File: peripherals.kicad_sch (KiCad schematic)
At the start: 10 parts, among them J10 perslot3ad, J11 perslot4ad, J12 perslot3c, J13 perslot4c, J14 peridcad, J15 peridcc, J6 perslot1ad, J7 perslot1c, J8 perslot2ad, J9 perslot2c

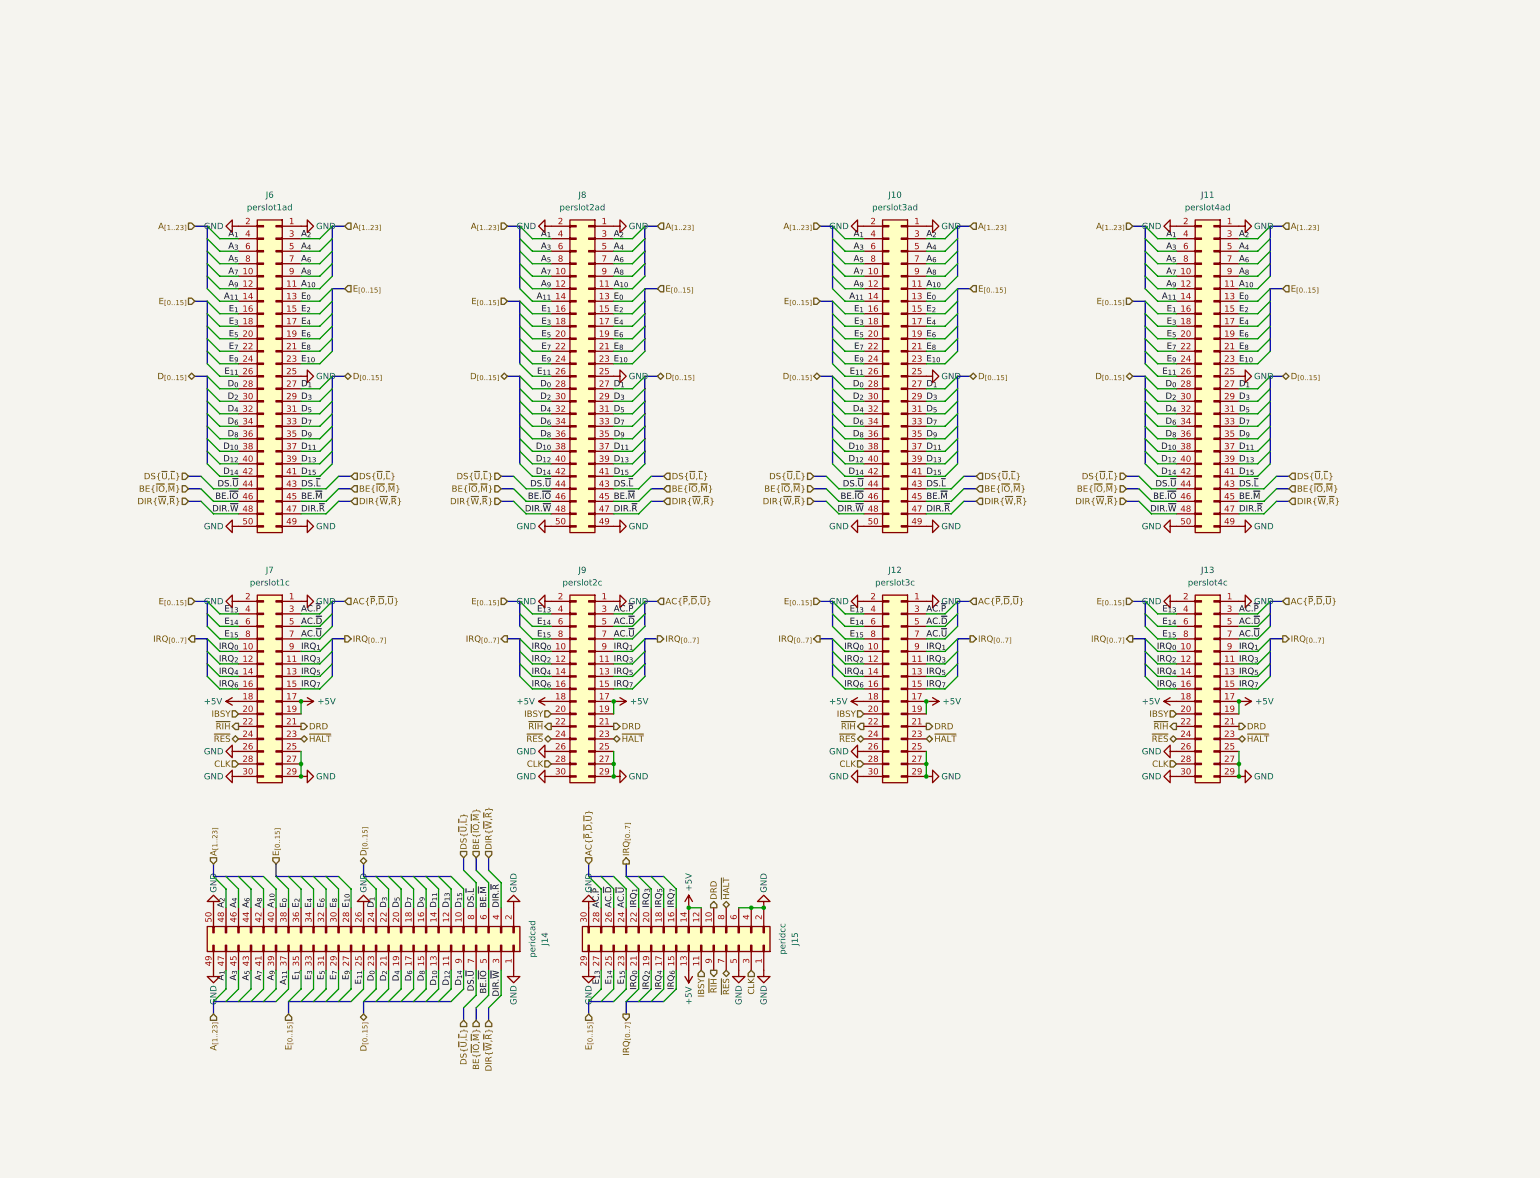
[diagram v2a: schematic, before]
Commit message: first commit: scheme ok [decoder]: 	- new spv. address space [mmu]: 	- removed pidreg 	- switched back to 8Kb mmu rams [ram/peripherals]: 	- added ground pins to connectors [misc]: 	- added DMA support 	- added clock halfer
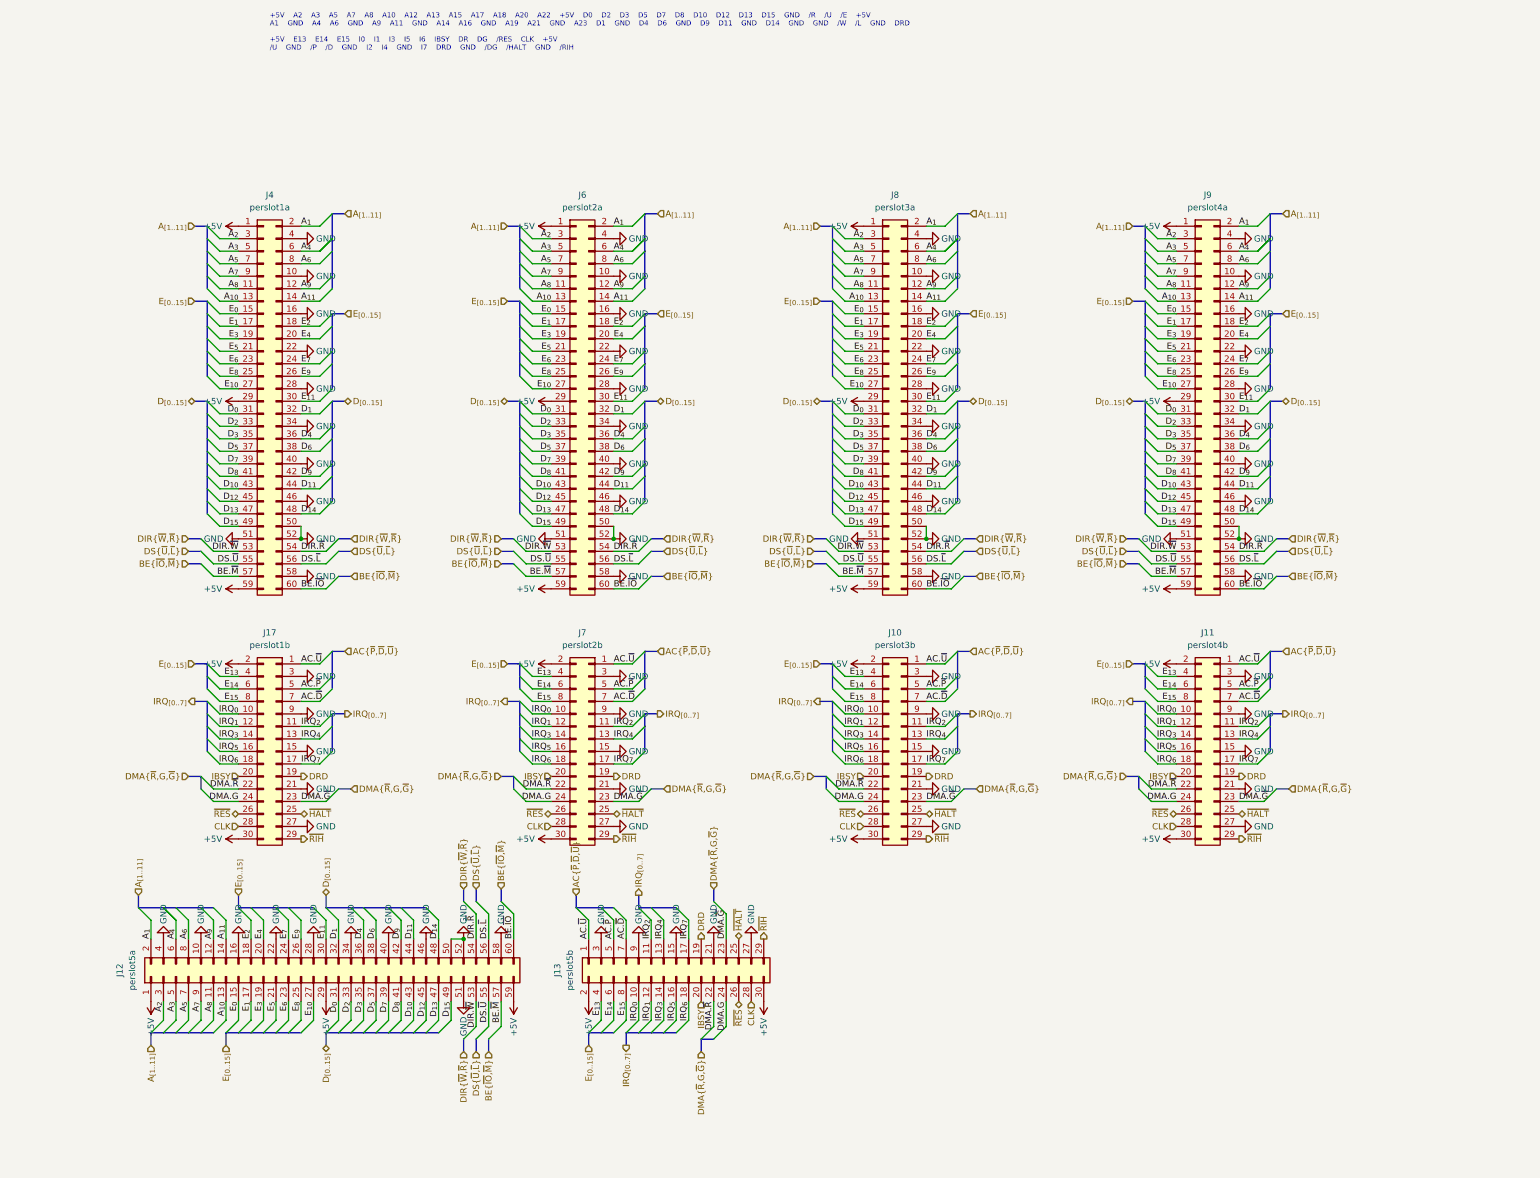
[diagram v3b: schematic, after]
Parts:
- removed J10: perslot3ad, Connector_PCBEdge:TE_1-5530843-6, symbol Connector_Generic:Conn_02x25_Odd_Even
- removed J11: perslot4ad, Connector_PCBEdge:TE_1-5530843-6, symbol Connector_Generic:Conn_02x25_Odd_Even
- removed J12: perslot3c, Connector_PCBEdge:55308432, symbol Connector_Generic:Conn_02x15_Odd_Even
- removed J14: peridcad, Connector_IDC:IDC-Header_2x25_P2.54mm_Horizontal, symbol Connector_Generic:Conn_02x25_Odd_Even
- removed J15: peridcc, Connector_IDC:IDC-Header_2x15_P2.54mm_Horizontal, symbol Connector_Generic:Conn_02x15_Odd_Even
- removed J6: perslot1ad, Connector_PCBEdge:TE_1-5530843-6, symbol Connector_Generic:Conn_02x25_Odd_Even
- removed J8: perslot2ad, Connector_PCBEdge:TE_1-5530843-6, symbol Connector_Generic:Conn_02x25_Odd_Even
- removed J9: perslot2c, Connector_PCBEdge:55308432, symbol Connector_Generic:Conn_02x15_Odd_Even
- added J10: perslot3b, Connector_PCBEdge:55308432, symbol Connector_Generic:Conn_02x15_Odd_Even
- added J11: perslot4b, Connector_PCBEdge:55308432, symbol Connector_Generic:Conn_02x15_Odd_Even
- added J12: perslot5a, symbol Connector_Generic:Conn_02x30_Odd_Even
- added J17: perslot1b, Connector_PCBEdge:55308432, symbol Connector_Generic:Conn_02x15_Odd_Even
- added J4: perslot1a, symbol Connector_Generic:Conn_02x30_Odd_Even
- added J6: perslot2a, symbol Connector_Generic:Conn_02x30_Odd_Even
- added J8: perslot3a, symbol Connector_Generic:Conn_02x30_Odd_Even
- added J9: perslot4a, symbol Connector_Generic:Conn_02x30_Odd_Even
- J13: value perslot4c -> perslot5b
- J7: value perslot1c -> perslot2b
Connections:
- net +5V: now also J13.2 (Pin_2), J13.30 (Pin_30), J7.2 (Pin_2), J7.30 (Pin_30), J10.2 (Pin_2), J10.30 (Pin_30), J11.2 (Pin_2), J11.30 (Pin_30), J12.1 (Pin_1), J12.29 (Pin_29), J12.59 (Pin_59), J17.2 (Pin_2), J17.30 (Pin_30), J4.1 (Pin_1), J4.29 (Pin_29), J4.59 (Pin_59), J6.1 (Pin_1), J6.29 (Pin_29), J6.59 (Pin_59), J8.1 (Pin_1), J8.29 (Pin_29), J8.59 (Pin_59), J9.1 (Pin_1), J9.29 (Pin_29), J9.59 (Pin_59); no longer J13.17 (Pin_17), J13.18 (Pin_18), J13.19 (Pin_19), J7.17 (Pin_17), J7.18 (Pin_18), J7.19 (Pin_19)
- net AC.~{D}: now also J13.7 (Pin_7), J7.7 (Pin_7), J10.7 (Pin_7), J11.7 (Pin_7), J17.7 (Pin_7); no longer J13.5 (Pin_5), J7.5 (Pin_5)
- net AC.~{P}: now also J13.5 (Pin_5), J7.5 (Pin_5), J10.5 (Pin_5), J11.5 (Pin_5), J17.5 (Pin_5); no longer J13.3 (Pin_3), J7.3 (Pin_3)
- net AC.~{U}: now also J13.1 (Pin_1), J7.1 (Pin_1), J10.1 (Pin_1), J11.1 (Pin_1), J17.1 (Pin_1); no longer J13.7 (Pin_7), J7.7 (Pin_7)
- net A_{10}: now also J12.13 (Pin_13), J4.13 (Pin_13), J6.13 (Pin_13), J8.13 (Pin_13), J9.13 (Pin_13)
- net A_{11}: now also J12.14 (Pin_14), J4.14 (Pin_14), J6.14 (Pin_14), J8.14 (Pin_14), J9.14 (Pin_14)
- net A_{1}: now also J12.2 (Pin_2), J4.2 (Pin_2), J6.2 (Pin_2), J8.2 (Pin_2), J9.2 (Pin_2)
- net A_{2}: now also J12.3 (Pin_3), J4.3 (Pin_3), J6.3 (Pin_3), J8.3 (Pin_3), J9.3 (Pin_3)
- net A_{3}: now also J12.5 (Pin_5), J4.5 (Pin_5), J6.5 (Pin_5), J8.5 (Pin_5), J9.5 (Pin_5)
- net A_{4}: now also J12.6 (Pin_6), J4.6 (Pin_6), J6.6 (Pin_6), J8.6 (Pin_6), J9.6 (Pin_6)
- net A_{5}: now also J12.7 (Pin_7), J4.7 (Pin_7), J6.7 (Pin_7), J8.7 (Pin_7), J9.7 (Pin_7)
- net A_{6}: now also J12.8 (Pin_8), J4.8 (Pin_8), J6.8 (Pin_8), J8.8 (Pin_8), J9.8 (Pin_8)
- net A_{7}: now also J12.9 (Pin_9), J4.9 (Pin_9), J6.9 (Pin_9), J8.9 (Pin_9), J9.9 (Pin_9)
- net A_{8}: now also J12.11 (Pin_11), J4.11 (Pin_11), J6.11 (Pin_11), J8.11 (Pin_11), J9.11 (Pin_11)
- net A_{9}: now also J12.12 (Pin_12), J4.12 (Pin_12), J6.12 (Pin_12), J8.12 (Pin_12), J9.12 (Pin_12)
- net BE.~{IO}: now also J12.60 (Pin_60), J4.60 (Pin_60), J6.60 (Pin_60), J8.60 (Pin_60), J9.60 (Pin_60)
- net BE.~{M}: now also J12.57 (Pin_57), J4.57 (Pin_57), J6.57 (Pin_57), J8.57 (Pin_57), J9.57 (Pin_57)
- net CLK: now also J10.28 (Pin_28), J11.28 (Pin_28), J17.28 (Pin_28)
- net DIR.~{R}: now also J12.54 (Pin_54), J4.54 (Pin_54), J6.54 (Pin_54), J8.54 (Pin_54), J9.54 (Pin_54)
- net DIR.~{W}: now also J12.53 (Pin_53), J4.53 (Pin_53), J6.53 (Pin_53), J8.53 (Pin_53), J9.53 (Pin_53)
- net DRD: now also J13.19 (Pin_19), J7.19 (Pin_19), J10.19 (Pin_19), J11.19 (Pin_19), J17.19 (Pin_19); no longer J13.21 (Pin_21), J7.21 (Pin_21)
- net DS.~{L}: now also J12.56 (Pin_56), J4.56 (Pin_56), J6.56 (Pin_56), J8.56 (Pin_56), J9.56 (Pin_56)
- net DS.~{U}: now also J12.55 (Pin_55), J4.55 (Pin_55), J6.55 (Pin_55), J8.55 (Pin_55), J9.55 (Pin_55)
- net D_{0}: now also J12.31 (Pin_31), J4.31 (Pin_31), J6.31 (Pin_31), J8.31 (Pin_31), J9.31 (Pin_31)
- net D_{10}: now also J12.43 (Pin_43), J4.43 (Pin_43), J6.43 (Pin_43), J8.43 (Pin_43), J9.43 (Pin_43)
- net D_{11}: now also J12.44 (Pin_44), J4.44 (Pin_44), J6.44 (Pin_44), J8.44 (Pin_44), J9.44 (Pin_44)
- net D_{12}: now also J12.45 (Pin_45), J4.45 (Pin_45), J6.45 (Pin_45), J8.45 (Pin_45), J9.45 (Pin_45)
- net D_{13}: now also J12.47 (Pin_47), J4.47 (Pin_47), J6.47 (Pin_47), J8.47 (Pin_47), J9.47 (Pin_47)
- net D_{14}: now also J12.48 (Pin_48), J4.48 (Pin_48), J6.48 (Pin_48), J8.48 (Pin_48), J9.48 (Pin_48)
- net D_{15}: now also J12.49 (Pin_49), J4.49 (Pin_49), J6.49 (Pin_49), J8.49 (Pin_49), J9.49 (Pin_49)
- net D_{1}: now also J12.32 (Pin_32), J4.32 (Pin_32), J6.32 (Pin_32), J8.32 (Pin_32), J9.32 (Pin_32)
- net D_{2}: now also J12.33 (Pin_33), J4.33 (Pin_33), J6.33 (Pin_33), J8.33 (Pin_33), J9.33 (Pin_33)
- net D_{3}: now also J12.35 (Pin_35), J4.35 (Pin_35), J6.35 (Pin_35), J8.35 (Pin_35), J9.35 (Pin_35)
- net D_{4}: now also J12.36 (Pin_36), J4.36 (Pin_36), J6.36 (Pin_36), J8.36 (Pin_36), J9.36 (Pin_36)
- net D_{5}: now also J12.37 (Pin_37), J4.37 (Pin_37), J6.37 (Pin_37), J8.37 (Pin_37), J9.37 (Pin_37)
- net D_{6}: now also J12.38 (Pin_38), J4.38 (Pin_38), J6.38 (Pin_38), J8.38 (Pin_38), J9.38 (Pin_38)
- net D_{7}: now also J12.39 (Pin_39), J4.39 (Pin_39), J6.39 (Pin_39), J8.39 (Pin_39), J9.39 (Pin_39)
- net D_{8}: now also J12.41 (Pin_41), J4.41 (Pin_41), J6.41 (Pin_41), J8.41 (Pin_41), J9.41 (Pin_41)
- net D_{9}: now also J12.42 (Pin_42), J4.42 (Pin_42), J6.42 (Pin_42), J8.42 (Pin_42), J9.42 (Pin_42)
- net E_{0}: now also J12.15 (Pin_15), J4.15 (Pin_15), J6.15 (Pin_15), J8.15 (Pin_15), J9.15 (Pin_15)
- net E_{10}: now also J12.27 (Pin_27), J4.27 (Pin_27), J6.27 (Pin_27), J8.27 (Pin_27), J9.27 (Pin_27)
- net E_{11}: now also J12.30 (Pin_30), J4.30 (Pin_30), J6.30 (Pin_30), J8.30 (Pin_30), J9.30 (Pin_30)
- net E_{13}: now also J10.4 (Pin_4), J11.4 (Pin_4), J17.4 (Pin_4)
- net E_{14}: now also J10.6 (Pin_6), J11.6 (Pin_6), J17.6 (Pin_6)
- net E_{15}: now also J10.8 (Pin_8), J11.8 (Pin_8), J17.8 (Pin_8)
- net E_{1}: now also J12.17 (Pin_17), J4.17 (Pin_17), J6.17 (Pin_17), J8.17 (Pin_17), J9.17 (Pin_17)
- net E_{2}: now also J12.18 (Pin_18), J4.18 (Pin_18), J6.18 (Pin_18), J8.18 (Pin_18), J9.18 (Pin_18)
- net E_{3}: now also J12.19 (Pin_19), J4.19 (Pin_19), J6.19 (Pin_19), J8.19 (Pin_19), J9.19 (Pin_19)
- net E_{4}: now also J12.20 (Pin_20), J4.20 (Pin_20), J6.20 (Pin_20), J8.20 (Pin_20), J9.20 (Pin_20)
- net E_{5}: now also J12.21 (Pin_21), J4.21 (Pin_21), J6.21 (Pin_21), J8.21 (Pin_21), J9.21 (Pin_21)
- net E_{6}: now also J12.23 (Pin_23), J4.23 (Pin_23), J6.23 (Pin_23), J8.23 (Pin_23), J9.23 (Pin_23)
- net E_{7}: now also J12.24 (Pin_24), J4.24 (Pin_24), J6.24 (Pin_24), J8.24 (Pin_24), J9.24 (Pin_24)
- net E_{8}: now also J12.25 (Pin_25), J4.25 (Pin_25), J6.25 (Pin_25), J8.25 (Pin_25), J9.25 (Pin_25)
- net E_{9}: now also J12.26 (Pin_26), J4.26 (Pin_26), J6.26 (Pin_26), J8.26 (Pin_26), J9.26 (Pin_26)
- net GND: now also J13.15 (Pin_15), J13.21 (Pin_21), J13.3 (Pin_3), J13.9 (Pin_9), J7.15 (Pin_15), J7.21 (Pin_21), J7.3 (Pin_3), J7.9 (Pin_9), J10.15 (Pin_15), J10.21 (Pin_21), J10.27 (Pin_27), J10.3 (Pin_3), J10.9 (Pin_9), J11.15 (Pin_15), J11.21 (Pin_21), J11.27 (Pin_27), J11.3 (Pin_3), J11.9 (Pin_9), J12.10 (Pin_10), J12.16 (Pin_16), J12.22 (Pin_22), J12.28 (Pin_28), J12.34 (Pin_34), J12.4 (Pin_4), J12.40 (Pin_40), J12.46 (Pin_46), J12.50 (Pin_50), J12.51 (Pin_51), J12.52 (Pin_52), J12.58 (Pin_58), J17.15 (Pin_15), J17.21 (Pin_21), J17.27 (Pin_27), J17.3 (Pin_3), J17.9 (Pin_9), J4.10 (Pin_10), J4.16 (Pin_16), J4.22 (Pin_22), J4.28 (Pin_28), J4.34 (Pin_34), J4.4 (Pin_4), J4.40 (Pin_40), J4.46 (Pin_46), J4.50 (Pin_50), J4.51 (Pin_51), J4.52 (Pin_52), J4.58 (Pin_58), J6.10 (Pin_10), J6.16 (Pin_16), J6.22 (Pin_22), J6.28 (Pin_28), J6.34 (Pin_34), J6.4 (Pin_4), J6.40 (Pin_40), J6.46 (Pin_46), J6.50 (Pin_50), J6.51 (Pin_51), J6.52 (Pin_52), J6.58 (Pin_58), J8.10 (Pin_10), J8.16 (Pin_16), J8.22 (Pin_22), J8.28 (Pin_28), J8.34 (Pin_34), J8.4 (Pin_4), J8.40 (Pin_40), J8.46 (Pin_46), J8.50 (Pin_50), J8.51 (Pin_51), J8.52 (Pin_52), J8.58 (Pin_58), J9.10 (Pin_10), J9.16 (Pin_16), J9.22 (Pin_22), J9.28 (Pin_28), J9.34 (Pin_34), J9.4 (Pin_4), J9.40 (Pin_40), J9.46 (Pin_46), J9.50 (Pin_50), J9.51 (Pin_51), J9.52 (Pin_52), J9.58 (Pin_58); no longer J13.1 (Pin_1), J13.2 (Pin_2), J13.25 (Pin_25), J13.26 (Pin_26), J13.29 (Pin_29), J13.30 (Pin_30), J7.1 (Pin_1), J7.2 (Pin_2), J7.25 (Pin_25), J7.26 (Pin_26), J7.29 (Pin_29), J7.30 (Pin_30)
- net IBSY: now also J10.20 (Pin_20), J11.20 (Pin_20), J17.20 (Pin_20)
- net IRQ_{0}: now also J10.10 (Pin_10), J11.10 (Pin_10), J17.10 (Pin_10)
- net IRQ_{1}: now also J13.12 (Pin_12), J7.12 (Pin_12), J10.12 (Pin_12), J11.12 (Pin_12), J17.12 (Pin_12); no longer J13.9 (Pin_9), J7.9 (Pin_9)
- net IRQ_{2}: now also J13.11 (Pin_11), J7.11 (Pin_11), J10.11 (Pin_11), J11.11 (Pin_11), J17.11 (Pin_11); no longer J13.12 (Pin_12), J7.12 (Pin_12)
- net IRQ_{3}: now also J13.14 (Pin_14), J7.14 (Pin_14), J10.14 (Pin_14), J11.14 (Pin_14), J17.14 (Pin_14); no longer J13.11 (Pin_11), J7.11 (Pin_11)
- net IRQ_{4}: now also J13.13 (Pin_13), J7.13 (Pin_13), J10.13 (Pin_13), J11.13 (Pin_13), J17.13 (Pin_13); no longer J13.14 (Pin_14), J7.14 (Pin_14)
- net IRQ_{5}: now also J13.16 (Pin_16), J7.16 (Pin_16), J10.16 (Pin_16), J11.16 (Pin_16), J17.16 (Pin_16); no longer J13.13 (Pin_13), J7.13 (Pin_13)
- net IRQ_{6}: now also J13.18 (Pin_18), J7.18 (Pin_18), J10.18 (Pin_18), J11.18 (Pin_18), J17.18 (Pin_18); no longer J13.16 (Pin_16), J7.16 (Pin_16)
- net IRQ_{7}: now also J13.17 (Pin_17), J7.17 (Pin_17), J10.17 (Pin_17), J11.17 (Pin_17), J17.17 (Pin_17); no longer J13.15 (Pin_15), J7.15 (Pin_15)
- net ~{HALT}: now also J13.25 (Pin_25), J7.25 (Pin_25), J10.25 (Pin_25), J11.25 (Pin_25), J17.25 (Pin_25); no longer J13.23 (Pin_23), J7.23 (Pin_23)
- net ~{RES}: now also J13.26 (Pin_26), J7.26 (Pin_26), J10.26 (Pin_26), J11.26 (Pin_26), J17.26 (Pin_26); no longer J13.24 (Pin_24), J7.24 (Pin_24)
- net ~{RIH}: now also J13.29 (Pin_29), J7.29 (Pin_29), J10.29 (Pin_29), J11.29 (Pin_29), J17.29 (Pin_29); no longer J13.22 (Pin_22), J7.22 (Pin_22)
- new net DMA.G: J10.24 (Pin_24), J11.24 (Pin_24), J13.24 (Pin_24), J17.24 (Pin_24), J7.24 (Pin_24)
- new net DMA.~{G}: J10.23 (Pin_23), J11.23 (Pin_23), J13.23 (Pin_23), J17.23 (Pin_23), J7.23 (Pin_23)
- new net DMA.~{R}: J10.22 (Pin_22), J11.22 (Pin_22), J13.22 (Pin_22), J17.22 (Pin_22), J7.22 (Pin_22)
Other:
- note added: "+5V A2 A3 A5 A7 A8 A10 A12 A13 A15 A17 A18 A20 A22 +5V D0 D2 D3 D5 D7 D8 D10 D12 D13 D15 GND /R /U /E +5V A1 GND A4 A6 GND A9 A11 GND A14 A16 GND A19 A21 GND A23 D1 GND D4 D6 GND D9 D11 GND D14 GND GND /W /L GND DRD +5V E13 E14 E15 I0 I1 I3 I5 I6 IBSY DR DG /RES CLK +5V /U GND /P /D GND I2 I4 GND I7 DRD GND /DG /HALT GND /RIH"

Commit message: assigned footprints
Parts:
- J12: footprint (none) -> Connector_IDC:IDC-Header_2x30_P2.54mm_Horizontal
- J13: footprint Connector_PCBEdge:55308432 -> Connector_IDC:IDC-Header_2x15_P2.54mm_Horizontal
- J4, J6, J8, J9: footprint (none) -> Connector_TE-Connectivity:55308437
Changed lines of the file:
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@@
 			)
 		)
-		(property "Footprint" ""
+		(property "Footprint" "Connector_TE-Connectivity:55308437"
 			(at 176.53 62.23 0)
 			(effects
@@
 			)
 		)
-		(property "Footprint" ""
+		(property "Footprint" "Connector_TE-Connectivity:55308437"
 			(at 113.03 62.23 0)
 			(effects
@@
 			)
 		)
-		(property "Footprint" "Connector_PCBEdge:55308432"
+		(property "Footprint" "Connector_IDC:IDC-Header_2x15_P2.54mm_Horizontal"
 			(at 133.35 176.53 0)
 			(effects
@@
 			)
 		)
-		(property "Footprint" ""
+		(property "Footprint" "Connector_IDC:IDC-Header_2x30_P2.54mm_Horizontal"
 			(at 62.23 179.07 0)
 			(effects
@@
 			)
 		)
-		(property "Footprint" ""
+		(property "Footprint" "Connector_TE-Connectivity:55308437"
 			(at 49.53 62.23 0)
 			(effects
@@
 			)
 		)
-		(property "Footprint" ""
+		(property "Footprint" "Connector_TE-Connectivity:55308437"
 			(at 240.03 62.23 0)
 			(effects

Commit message: 1.0.0 commit
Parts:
- removed J12: perslot5a, Connector_IDC:IDC-Header_2x30_P2.54mm_Horizontal, symbol Connector_Generic:Conn_02x30_Odd_Even
- removed J13: perslot5b, Connector_IDC:IDC-Header_2x15_P2.54mm_Horizontal, symbol Connector_Generic:Conn_02x15_Odd_Even
- removed J6: perslot2a, Connector_TE-Connectivity:55308437, symbol Connector_Generic:Conn_02x30_Odd_Even
- removed J7: perslot2b, Connector_PCBEdge:55308432, symbol Connector_Generic:Conn_02x15_Odd_Even
- removed J9: perslot4a, Connector_TE-Connectivity:55308437, symbol Connector_Generic:Conn_02x30_Odd_Even
- added J1: perslot4a, Connector_TE-Connectivity:55308437, symbol Connector_Generic:Conn_02x30_Odd_Even
- added J12: perslot2b, Connector_PCBEdge:55308432, symbol Connector_Generic:Conn_02x15_Odd_Even
- added J15: perslot5b, Connector_IDC:IDC-Header_2x15_P2.54mm_Horizontal, symbol Connector_Generic:Conn_02x15_Odd_Even
- added J2: perslot3a, Connector_TE-Connectivity:55308437, symbol Connector_Generic:Conn_02x30_Odd_Even
- added J3: perslot2a, Connector_TE-Connectivity:55308437, symbol Connector_Generic:Conn_02x30_Odd_Even
- J10: value perslot3b -> perslot4b
- J11: value perslot4b -> perslot3b
- J8: value perslot3a -> perslot5a; footprint Connector_TE-Connectivity:55308437 -> Connector_IDC:IDC-Header_2x30_P2.54mm_Horizontal
- renumbered J17 to J13
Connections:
- net +5V: now also J8.31 (Pin_31), J1.1 (Pin_1), J1.29 (Pin_29), J1.59 (Pin_59), J12.2 (Pin_2), J12.30 (Pin_30), J15.1 (Pin_1), J15.29 (Pin_29), J2.1 (Pin_1), J2.29 (Pin_29), J2.59 (Pin_59), J3.1 (Pin_1), J3.29 (Pin_29), J3.59 (Pin_59); no longer J8.29 (Pin_29)
- net AC.~{D}: now also J12.7 (Pin_7), J15.24 (Pin_24)
- net AC.~{P}: now also J12.5 (Pin_5), J15.26 (Pin_26)
- net AC.~{U}: now also J10.8 (Pin_8), J11.8 (Pin_8), J13.8 (Pin_8), J12.8 (Pin_8), J15.23 (Pin_23); no longer J10.1 (Pin_1), J11.1 (Pin_1), J13.1 (Pin_1)
- net A_{10}: now also J8.47 (Pin_47), J1.13 (Pin_13), J2.13 (Pin_13), J3.13 (Pin_13); no longer J8.13 (Pin_13)
- net A_{11}: now also J8.48 (Pin_48), J1.14 (Pin_14), J2.14 (Pin_14), J3.14 (Pin_14); no longer J8.14 (Pin_14)
- net A_{1}: now also J8.60 (Pin_60), J1.2 (Pin_2), J2.2 (Pin_2), J3.2 (Pin_2); no longer J8.2 (Pin_2)
- net A_{2}: now also J8.57 (Pin_57), J1.3 (Pin_3), J2.3 (Pin_3), J3.3 (Pin_3); no longer J8.3 (Pin_3)
- net A_{3}: now also J8.55 (Pin_55), J1.5 (Pin_5), J2.5 (Pin_5), J3.5 (Pin_5); no longer J8.5 (Pin_5)
- net A_{4}: now also J8.56 (Pin_56), J1.6 (Pin_6), J2.6 (Pin_6), J3.6 (Pin_6); no longer J8.6 (Pin_6)
- net A_{5}: now also J8.53 (Pin_53), J1.7 (Pin_7), J2.7 (Pin_7), J3.7 (Pin_7); no longer J8.7 (Pin_7)
- net A_{6}: now also J8.54 (Pin_54), J1.8 (Pin_8), J2.8 (Pin_8), J3.8 (Pin_8); no longer J8.8 (Pin_8)
- net A_{7}: now also J8.51 (Pin_51), J1.9 (Pin_9), J2.9 (Pin_9), J3.9 (Pin_9); no longer J8.9 (Pin_9)
- net A_{8}: now also J8.49 (Pin_49), J1.11 (Pin_11), J2.11 (Pin_11), J3.11 (Pin_11); no longer J8.11 (Pin_11)
- net A_{9}: now also J8.50 (Pin_50), J1.12 (Pin_12), J2.12 (Pin_12), J3.12 (Pin_12); no longer J8.12 (Pin_12)
- net BE.~{IO}: now also J4.50 (Pin_50), J8.12 (Pin_12), J1.50 (Pin_50), J2.50 (Pin_50), J3.50 (Pin_50); no longer J4.60 (Pin_60), J8.60 (Pin_60)
- net BE.~{M}: now also J4.51 (Pin_51), J8.9 (Pin_9), J1.51 (Pin_51), J2.51 (Pin_51), J3.51 (Pin_51); no longer J4.57 (Pin_57), J8.57 (Pin_57)
- net CLK: now also J10.16 (Pin_16), J11.16 (Pin_16), J13.16 (Pin_16), J12.16 (Pin_16), J15.15 (Pin_15); no longer J10.28 (Pin_28), J11.28 (Pin_28), J13.28 (Pin_28)
- net DIR.~{R}: now also J8.8 (Pin_8), J1.54 (Pin_54), J2.54 (Pin_54), J3.54 (Pin_54); no longer J8.54 (Pin_54)
- net DIR.~{W}: now also J8.7 (Pin_7), J1.53 (Pin_53), J2.53 (Pin_53), J3.53 (Pin_53); no longer J8.53 (Pin_53)
- net DMA.G: now also J10.13 (Pin_13), J11.13 (Pin_13), J13.13 (Pin_13), J12.13 (Pin_13), J15.18 (Pin_18); no longer J10.24 (Pin_24), J11.24 (Pin_24), J13.24 (Pin_24)
- net DMA.~{G}: now also J10.11 (Pin_11), J11.11 (Pin_11), J13.11 (Pin_11), J12.11 (Pin_11), J15.20 (Pin_20); no longer J10.23 (Pin_23), J11.23 (Pin_23), J13.23 (Pin_23)
- net DMA.~{R}: now also J10.12 (Pin_12), J11.12 (Pin_12), J13.12 (Pin_12), J12.12 (Pin_12), J15.19 (Pin_19); no longer J10.22 (Pin_22), J11.22 (Pin_22), J13.22 (Pin_22)
- net DRD: now also J4.60 (Pin_60), J8.2 (Pin_2), J1.60 (Pin_60), J2.60 (Pin_60), J3.60 (Pin_60); no longer J10.19 (Pin_19), J11.19 (Pin_19), J13.19 (Pin_19)
- net DS.~{L}: now also J8.6 (Pin_6), J1.56 (Pin_56), J2.56 (Pin_56), J3.56 (Pin_56); no longer J8.56 (Pin_56)
- net DS.~{U}: now also J8.5 (Pin_5), J1.55 (Pin_55), J2.55 (Pin_55), J3.55 (Pin_55); no longer J8.55 (Pin_55)
- net D_{0}: now also J8.29 (Pin_29), J1.31 (Pin_31), J2.31 (Pin_31), J3.31 (Pin_31); no longer J8.31 (Pin_31)
- net D_{10}: now also J8.17 (Pin_17), J1.43 (Pin_43), J2.43 (Pin_43), J3.43 (Pin_43); no longer J8.43 (Pin_43)
- net D_{11}: now also J8.18 (Pin_18), J1.44 (Pin_44), J2.44 (Pin_44), J3.44 (Pin_44); no longer J8.44 (Pin_44)
- net D_{12}: now also J8.15 (Pin_15), J1.45 (Pin_45), J2.45 (Pin_45), J3.45 (Pin_45); no longer J8.45 (Pin_45)
- net D_{13}: now also J8.13 (Pin_13), J1.47 (Pin_47), J2.47 (Pin_47), J3.47 (Pin_47); no longer J8.47 (Pin_47)
- net D_{14}: now also J8.14 (Pin_14), J1.48 (Pin_48), J2.48 (Pin_48), J3.48 (Pin_48); no longer J8.48 (Pin_48)
- net D_{15}: now also J8.11 (Pin_11), J1.49 (Pin_49), J2.49 (Pin_49), J3.49 (Pin_49); no longer J8.49 (Pin_49)
- net D_{1}: now also J8.30 (Pin_30), J1.32 (Pin_32), J2.32 (Pin_32), J3.32 (Pin_32); no longer J8.32 (Pin_32)
- net D_{2}: now also J8.27 (Pin_27), J1.33 (Pin_33), J2.33 (Pin_33), J3.33 (Pin_33); no longer J8.33 (Pin_33)
- net D_{3}: now also J8.25 (Pin_25), J1.35 (Pin_35), J2.35 (Pin_35), J3.35 (Pin_35); no longer J8.35 (Pin_35)
- net D_{4}: now also J8.26 (Pin_26), J1.36 (Pin_36), J2.36 (Pin_36), J3.36 (Pin_36); no longer J8.36 (Pin_36)
- net D_{5}: now also J8.23 (Pin_23), J1.37 (Pin_37), J2.37 (Pin_37), J3.37 (Pin_37); no longer J8.37 (Pin_37)
- net D_{6}: now also J8.24 (Pin_24), J1.38 (Pin_38), J2.38 (Pin_38), J3.38 (Pin_38); no longer J8.38 (Pin_38)
- net D_{7}: now also J8.21 (Pin_21), J1.39 (Pin_39), J2.39 (Pin_39), J3.39 (Pin_39); no longer J8.39 (Pin_39)
- net D_{8}: now also J8.19 (Pin_19), J1.41 (Pin_41), J2.41 (Pin_41), J3.41 (Pin_41); no longer J8.41 (Pin_41)
- net D_{9}: now also J8.20 (Pin_20), J1.42 (Pin_42), J2.42 (Pin_42), J3.42 (Pin_42); no longer J8.42 (Pin_42)
- net E_{0}: now also J8.45 (Pin_45), J1.15 (Pin_15), J2.15 (Pin_15), J3.15 (Pin_15); no longer J8.15 (Pin_15)
- net E_{10}: now also J8.33 (Pin_33), J1.27 (Pin_27), J2.27 (Pin_27), J3.27 (Pin_27); no longer J8.27 (Pin_27)
- net E_{11}: now also J8.32 (Pin_32), J1.30 (Pin_30), J2.30 (Pin_30), J3.30 (Pin_30); no longer J8.30 (Pin_30)
- net E_{13}: now also J10.1 (Pin_1), J11.1 (Pin_1), J13.1 (Pin_1), J12.1 (Pin_1), J15.30 (Pin_30); no longer J10.4 (Pin_4), J11.4 (Pin_4), J13.4 (Pin_4)
- net E_{14}: now also J10.4 (Pin_4), J11.4 (Pin_4), J13.4 (Pin_4), J12.4 (Pin_4), J15.27 (Pin_27); no longer J10.6 (Pin_6), J11.6 (Pin_6), J13.6 (Pin_6)
- net E_{15}: now also J10.6 (Pin_6), J11.6 (Pin_6), J13.6 (Pin_6), J12.6 (Pin_6), J15.25 (Pin_25); no longer J10.8 (Pin_8), J11.8 (Pin_8), J13.8 (Pin_8)
- net E_{1}: now also J8.43 (Pin_43), J1.17 (Pin_17), J2.17 (Pin_17), J3.17 (Pin_17); no longer J8.17 (Pin_17)
- net E_{2}: now also J8.44 (Pin_44), J1.18 (Pin_18), J2.18 (Pin_18), J3.18 (Pin_18); no longer J8.18 (Pin_18)
- net E_{3}: now also J8.41 (Pin_41), J1.19 (Pin_19), J2.19 (Pin_19), J3.19 (Pin_19); no longer J8.19 (Pin_19)
- net E_{4}: now also J8.42 (Pin_42), J1.20 (Pin_20), J2.20 (Pin_20), J3.20 (Pin_20); no longer J8.20 (Pin_20)
- net E_{5}: now also J8.39 (Pin_39), J1.21 (Pin_21), J2.21 (Pin_21), J3.21 (Pin_21); no longer J8.21 (Pin_21)
- net E_{6}: now also J8.37 (Pin_37), J1.23 (Pin_23), J2.23 (Pin_23), J3.23 (Pin_23); no longer J8.23 (Pin_23)
- net E_{7}: now also J8.38 (Pin_38), J1.24 (Pin_24), J2.24 (Pin_24), J3.24 (Pin_24); no longer J8.24 (Pin_24)
- net E_{8}: now also J8.35 (Pin_35), J1.25 (Pin_25), J2.25 (Pin_25), J3.25 (Pin_25); no longer J8.25 (Pin_25)
- net E_{9}: now also J8.36 (Pin_36), J1.26 (Pin_26), J2.26 (Pin_26), J3.26 (Pin_26); no longer J8.26 (Pin_26)
- net GND: now also J10.10 (Pin_10), J11.10 (Pin_10), J13.10 (Pin_10), J1.10 (Pin_10), J1.16 (Pin_16), J1.22 (Pin_22), J1.28 (Pin_28), J1.34 (Pin_34), J1.4 (Pin_4), J1.40 (Pin_40), J1.46 (Pin_46), J1.52 (Pin_52), J1.58 (Pin_58), J12.10 (Pin_10), J12.15 (Pin_15), J12.21 (Pin_21), J12.27 (Pin_27), J12.3 (Pin_3), J12.9 (Pin_9), J15.10 (Pin_10), J15.16 (Pin_16), J15.21 (Pin_21), J15.22 (Pin_22), J15.28 (Pin_28), J15.4 (Pin_4), J2.10 (Pin_10), J2.16 (Pin_16), J2.22 (Pin_22), J2.28 (Pin_28), J2.34 (Pin_34), J2.4 (Pin_4), J2.40 (Pin_40), J2.46 (Pin_46), J2.52 (Pin_52), J2.58 (Pin_58), J3.10 (Pin_10), J3.16 (Pin_16), J3.22 (Pin_22), J3.28 (Pin_28), J3.34 (Pin_34), J3.4 (Pin_4), J3.40 (Pin_40), J3.46 (Pin_46), J3.52 (Pin_52), J3.58 (Pin_58); no longer J4.50 (Pin_50), J4.51 (Pin_51), J8.50 (Pin_50), J8.51 (Pin_51)
- net IBSY: now also J10.29 (Pin_29), J11.29 (Pin_29), J13.29 (Pin_29), J12.29 (Pin_29), J15.2 (Pin_2); no longer J10.20 (Pin_20), J11.20 (Pin_20), J13.20 (Pin_20)
- net IRQ_{0}: now also J10.20 (Pin_20), J11.20 (Pin_20), J13.20 (Pin_20), J12.20 (Pin_20), J15.11 (Pin_11); no longer J10.10 (Pin_10), J11.10 (Pin_10), J13.10 (Pin_10)
- net IRQ_{1}: now also J10.19 (Pin_19), J11.19 (Pin_19), J13.19 (Pin_19), J12.19 (Pin_19), J15.12 (Pin_12); no longer J10.12 (Pin_12), J11.12 (Pin_12), J13.12 (Pin_12)
- net IRQ_{2}: now also J10.22 (Pin_22), J11.22 (Pin_22), J13.22 (Pin_22), J12.22 (Pin_22), J15.9 (Pin_9); no longer J10.11 (Pin_11), J11.11 (Pin_11), J13.11 (Pin_11)
- net IRQ_{3}: now also J10.24 (Pin_24), J11.24 (Pin_24), J13.24 (Pin_24), J12.24 (Pin_24), J15.7 (Pin_7); no longer J10.14 (Pin_14), J11.14 (Pin_14), J13.14 (Pin_14)
- net IRQ_{4}: now also J10.23 (Pin_23), J11.23 (Pin_23), J13.23 (Pin_23), J12.23 (Pin_23), J15.8 (Pin_8); no longer J10.13 (Pin_13), J11.13 (Pin_13), J13.13 (Pin_13)
- net IRQ_{5}: now also J10.26 (Pin_26), J11.26 (Pin_26), J13.26 (Pin_26), J12.26 (Pin_26), J15.5 (Pin_5); no longer J10.16 (Pin_16), J11.16 (Pin_16), J13.16 (Pin_16)
- net IRQ_{6}: now also J10.25 (Pin_25), J11.25 (Pin_25), J13.25 (Pin_25), J12.25 (Pin_25), J15.6 (Pin_6); no longer J10.18 (Pin_18), J11.18 (Pin_18), J13.18 (Pin_18)
- net IRQ_{7}: now also J10.28 (Pin_28), J11.28 (Pin_28), J13.28 (Pin_28), J12.28 (Pin_28), J15.3 (Pin_3); no longer J10.17 (Pin_17), J11.17 (Pin_17), J13.17 (Pin_17)
- net ~{HALT}: now also J10.17 (Pin_17), J11.17 (Pin_17), J13.17 (Pin_17), J12.17 (Pin_17), J15.14 (Pin_14); no longer J10.25 (Pin_25), J11.25 (Pin_25), J13.25 (Pin_25)
- net ~{RES}: now also J10.18 (Pin_18), J11.18 (Pin_18), J13.18 (Pin_18), J12.18 (Pin_18), J15.13 (Pin_13); no longer J10.26 (Pin_26), J11.26 (Pin_26), J13.26 (Pin_26)
- net ~{RIH}: now also J4.57 (Pin_57), J8.3 (Pin_3), J1.57 (Pin_57), J2.57 (Pin_57), J3.57 (Pin_57); no longer J10.29 (Pin_29), J11.29 (Pin_29), J13.29 (Pin_29)
- new net DMA.~{SAS}: J10.14 (Pin_14), J11.14 (Pin_14), J12.14 (Pin_14), J13.14 (Pin_14), J15.17 (Pin_17)
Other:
- moved on the sheet: J13, J4
